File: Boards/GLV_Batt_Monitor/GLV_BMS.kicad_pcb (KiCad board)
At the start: 2 copper layers, 76.2 x 67.3 mm, 44 parts, among them J1 CONN_02X03, J2 CONN_02X03, J3 MM_F_RA_20, U1 MCP2561-E_SN, U101 TPS560430YF, U2 ATMEGA16M1, U3 ATmega328P-AU, Y1 Crystal_SMD, Y2 Crystal_SMD

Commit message: Imported new DXF, uploading Rev 5
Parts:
- moved COUT103 5.88 mm to (170.9, 110.0)
- moved D101 5.88 mm to (172.8, 93.0)
- moved D102 5.88 mm to (176.9, 87.9)
- moved F101 5.88 mm to (170.8, 98.0)
- moved R104 5.88 mm to (166.9, 103.2)
- moved R105 5.88 mm to (163.1, 101.7)
- moved C102 5.88 mm to (174.4, 99.6)
- moved R101 5.88 mm to (173.0, 87.9)
- moved R103 5.88 mm to (177.5, 105.4)
- moved C101 5.88 mm to (174.6, 97.8)
- moved COUT101 5.88 mm to (173.2, 110.0)
- moved COUT102 5.88 mm to (166.9, 108.9)
- moved L101 5.88 mm to (170.8, 105.5)
- moved R102 5.88 mm to (177.5, 101.5)
- moved C103 5.88 mm to (174.5, 106.0)
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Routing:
- net /SCK_2: track 143.0 -> 138.3 mm
- net /SCK: track 86.8 -> 82.1 mm
- net /RESET_2: track 114.2 -> 110.2 mm
- net /MOSI: track 58.6 -> 54.7 mm, vias 4 -> 2
- net /MISO_2: track 136.7 -> 132.9 mm
- net GND: track 94.3 -> 90.6 mm
- net /MOSI_2: track 137.7 -> 134.2 mm
- net /MISO: track 71.2 -> 67.8 mm
- net /RESET: track 56.1 -> 53.0 mm
- net VCC: track 179.3 -> 177.0 mm
- net +12V: track 29.9 -> 28.4 mm
- net Net-(D103-Pad2): track 1.75 -> 2.79 mm
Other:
- outline, holes or cut-outs redrawn
- board text added: "Nabih Estefan GLV Battery Monitor Board 02/05/2020 - Rev 5 Mk V - OEM"
- board text removed: "Nabih Estefan GLV Battery Monitor Board 02/05/2020 - Rev 4 Mk V - OEM"

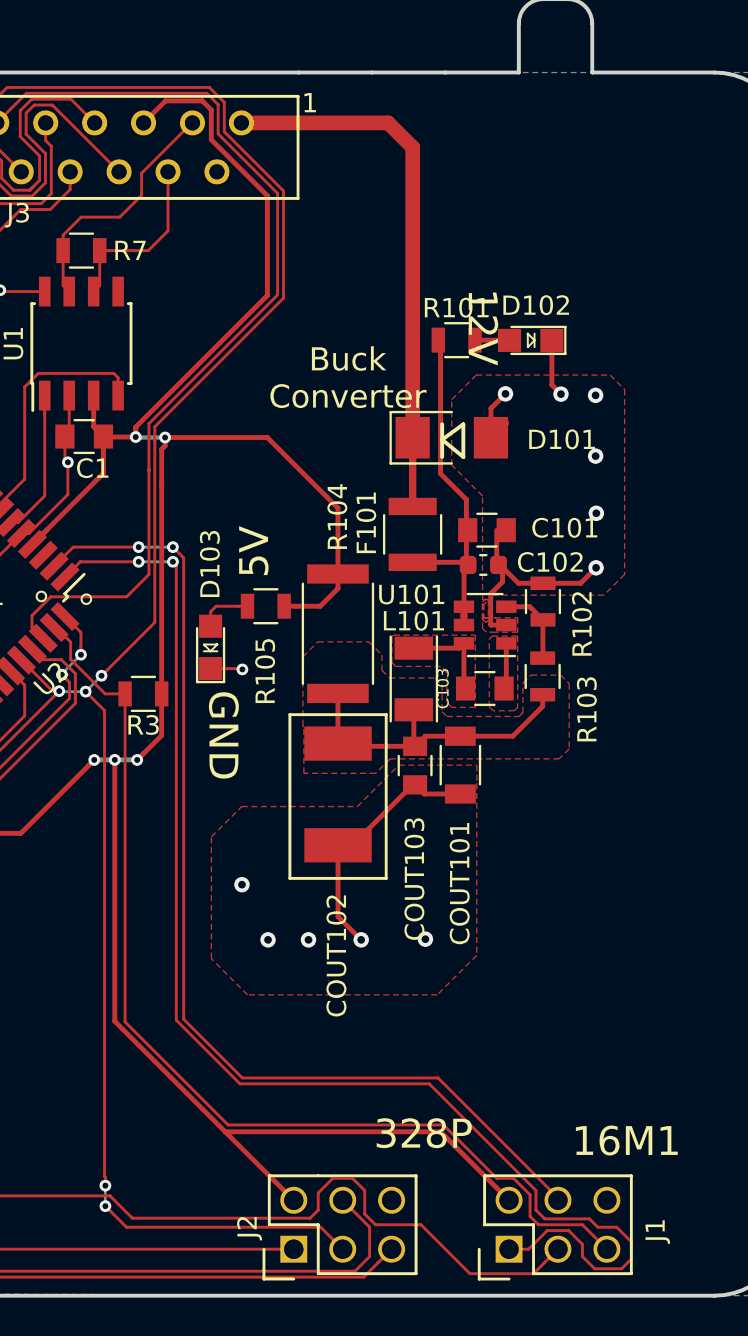
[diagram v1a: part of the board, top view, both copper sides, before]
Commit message: Revised version of Rev 5 with final edge cuts
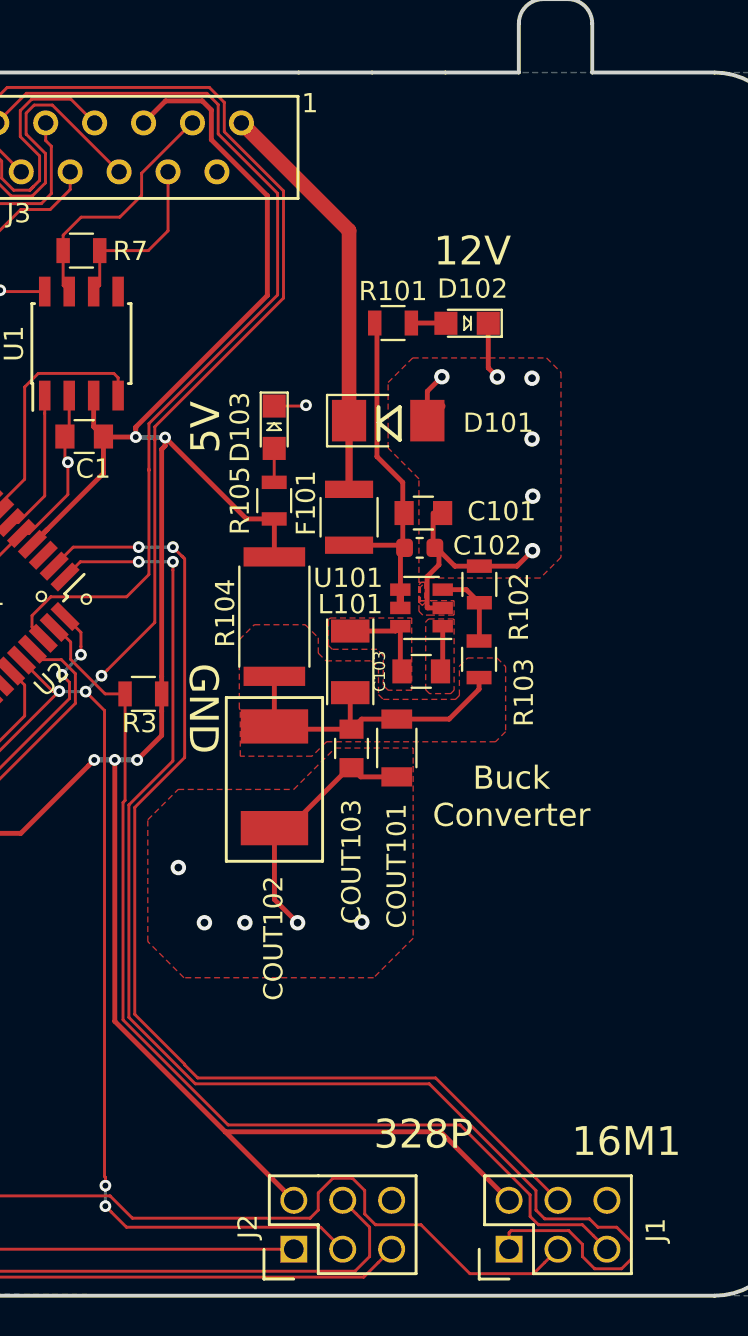
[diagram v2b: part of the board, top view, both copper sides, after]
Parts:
- moved D103 11.9 mm to (163.6, 92.5), turned to 270 degrees
- moved R105 5.50 mm to (163.6, 96.3), turned to 90 degrees
- moved L101 3.42 mm to (167.5, 104.6)
- moved C103 3.42 mm to (171.2, 105.1)
- moved COUT102 3.42 mm to (163.6, 108.0)
- moved U101 3.42 mm to (171.2, 101.8)
- moved C101 3.42 mm to (171.3, 96.9)
- moved F101 3.42 mm to (167.5, 97.1)
- moved R102 3.42 mm to (174.2, 100.6)
- moved C102 3.42 mm to (171.1, 98.7)
- moved COUT101 3.42 mm to (169.9, 109.1)
- moved COUT103 3.42 mm to (167.6, 109.1)
- moved D101 3.42 mm to (169.5, 92.1)
- moved D102 3.42 mm to (173.6, 87.1)
- moved R101 3.42 mm to (169.7, 87.0)
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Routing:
- net VCC: track 177.0 -> 168.4 mm
- net +12V: track 28.4 -> 21.6 mm
- net /MISO: track 67.8 -> 71.8 mm
- net /MOSI: track 54.7 -> 58.3 mm
- net Net-(D103-Pad2): track 2.79 -> 1.76 mm
